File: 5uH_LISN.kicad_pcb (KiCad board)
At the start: 2 copper layers, 112.4 x 60.5 mm, 78 parts, among them J1 Conn_Coaxial, J2 Conn_Coaxial, J3 BANANA_CONN, J4 BANANA_CONN, J5 BANANA_CONN, J6 BANANA_CONN, J7 BANANA_CONN, J8 BANANA_CONN

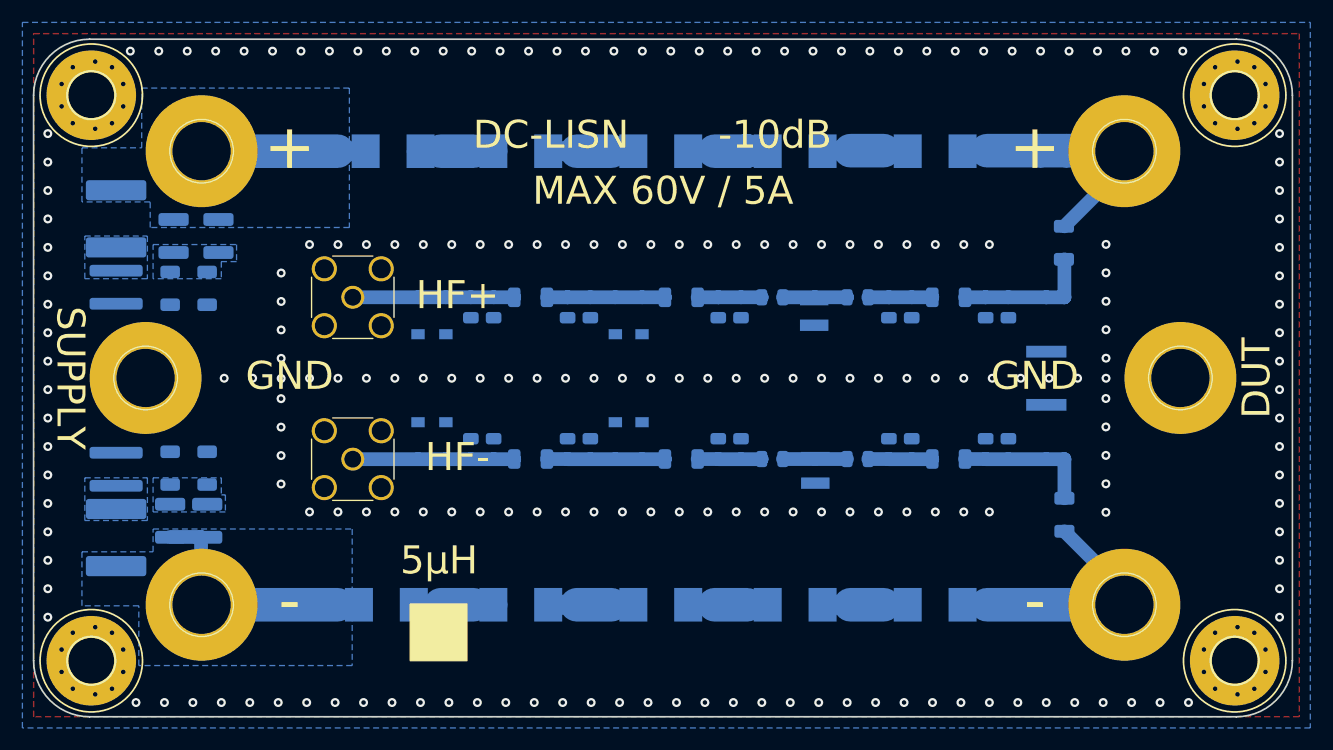
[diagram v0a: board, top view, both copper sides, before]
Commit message: LISN V1 R0 * Added simulation with LTSpice of the 10dB Attenuator / Transient Filter (with default 1N4148 and BAV99) * Replaced some 1N4148W by BAV99 from Nexperia (to reach up to 400MHz flat 10dB Attenuator / Transient Filter) * Changed space to have 19.06mm between Supply / DUT "+" <=> "GND" <=> "-" => 4mm BANANA JACK for BNC adapter * Changed Keystone Electronics 575-4 which are too short for banana by Keystone Electronics 575-8
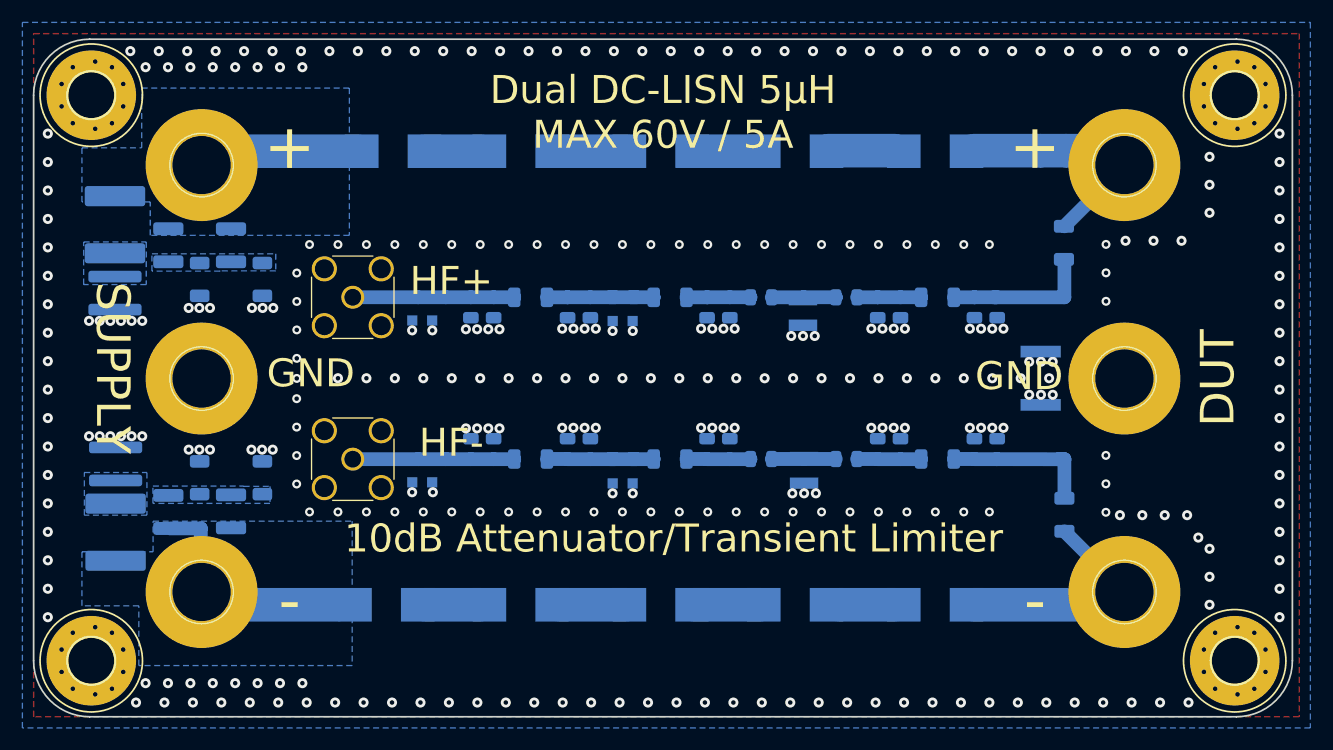
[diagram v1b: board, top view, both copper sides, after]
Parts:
- removed D5, D6, D7, D8: 1N4148W, Diode_SMD:D_SOD-123
- D1, D2, D3, D4: value 1N4148W -> SOT23-DIODEDUAL; footprint Diode_SMD:D_SOD-123 -> 5uH_LISN:SOT23-DIODEDUAL
- J1, J2: value Conn_Coaxial -> Conn_SMA
- moved D2 21.7 mm to (152.7, 104.1), turned to 0 degrees
- moved D4 16.0 mm to (152.7, 118.6), turned to 0 degrees
- moved D3 14.0 mm to (134.8, 118.5), turned to 0 degrees
- moved R14 5.01 mm to (120.5, 119.1)
- moved J4 5.00 mm to (115.1, 110.3)
- moved J6 5.00 mm to (197.5, 110.3)
- moved R9 5.00 mm to (120.5, 101.4)
- moved R31 3.03 mm to (184.1, 103.9)
- moved R10 2.77 mm to (114.9, 119.1)
- moved R13 2.75 mm to (114.9, 101.4)
- moved C8 2.29 mm to (117.7, 122.1)
- moved C5 1.39 mm to (117.7, 98.4)
- moved J3 1.24 mm to (115.1, 91.2)
- moved J7 1.24 mm to (197.5, 91.2)
- moved J5 1.14 mm to (115.1, 129.3)
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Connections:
- D1 pad 1: Net-(D1-Pad1) -> GND
- D2 pad 1: Net-(D2-Pad1) -> GND
- D3 pad 2: Net-(D1-Pad1) -> GND
- D4 pad 2: Net-(D2-Pad1) -> GND
- J1 pad 1: Net-(D1-Pad1) -> Net-(D1-Pad3)
- J2 pad 1: Net-(D2-Pad1) -> Net-(D3-Pad3)
- R1 pad 2: Net-(D1-Pad1) -> Net-(D1-Pad3)
- R11 pad 2: Net-(D5-Pad1) -> Net-(D2-Pad3)
- R12 pad 2: Net-(D6-Pad1) -> Net-(D4-Pad3)
- R15 pad 2: Net-(D5-Pad1) -> Net-(D2-Pad3)
- R16 pad 2: Net-(D6-Pad1) -> Net-(D4-Pad3)
- R17 pad 1: Net-(D5-Pad1) -> Net-(D2-Pad3)
- R18 pad 1: Net-(D6-Pad1) -> Net-(D4-Pad3)
- R2 pad 2: Net-(D2-Pad1) -> Net-(D3-Pad3)
- R5 pad 2: Net-(D1-Pad1) -> Net-(D1-Pad3)
- R6 pad 2: Net-(D2-Pad1) -> Net-(D3-Pad3)
- R7 pad 1: Net-(D1-Pad1) -> Net-(D1-Pad3)
- R7 pad 2: Net-(D5-Pad1) -> Net-(D2-Pad3)
- R8 pad 1: Net-(D2-Pad1) -> Net-(D3-Pad3)
- R8 pad 2: Net-(D6-Pad1) -> Net-(D4-Pad3)
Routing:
- net Net-(D3-Pad3): track 0.00 -> 14.4 mm
- net Net-(D2-Pad1): track 14.4 -> 0.00 mm
- net Net-(D1-Pad3): track 0.00 -> 14.4 mm
- net Net-(D1-Pad1): track 14.4 -> 0.00 mm
- net Net-(D6-Pad1): track 10.5 -> 0.00 mm
- net Net-(D4-Pad3): track 0.00 -> 10.5 mm
- net Net-(D5-Pad1): track 10.5 -> 0.00 mm
- net Net-(D2-Pad3): track 0.00 -> 10.5 mm
- net Net-(L7-Pad2): track 7.24 -> 5.00 mm
- net Net-(L1-Pad2): track 7.24 -> 5.00 mm
- net Net-(L10-Pad2): track 7.30 -> 9.30 mm
- net Net-(C15-Pad1): track 24.1 -> 22.4 mm
- net Net-(C16-Pad2): track 12.4 -> 13.8 mm
- net Net-(L8-Pad2): track 7.41 -> 6.00 mm
- net Net-(L2-Pad2): track 7.41 -> 6.00 mm
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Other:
- board text added: "10dB Attenuator/Transient Limiter"
- board text added: "Dual DC-LISN 5µH"
- board text added: "V1 R0 05Dec2021"
- board text removed: "-10dB"
- board text removed: "5µH"
- board text removed: "DC-LISN"

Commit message: Fixed issue https://github.com/bvernoux/EMC_5uH_LISN/issues/4 Remove bottom layer soldermask on PCB edge for proper grounding to case
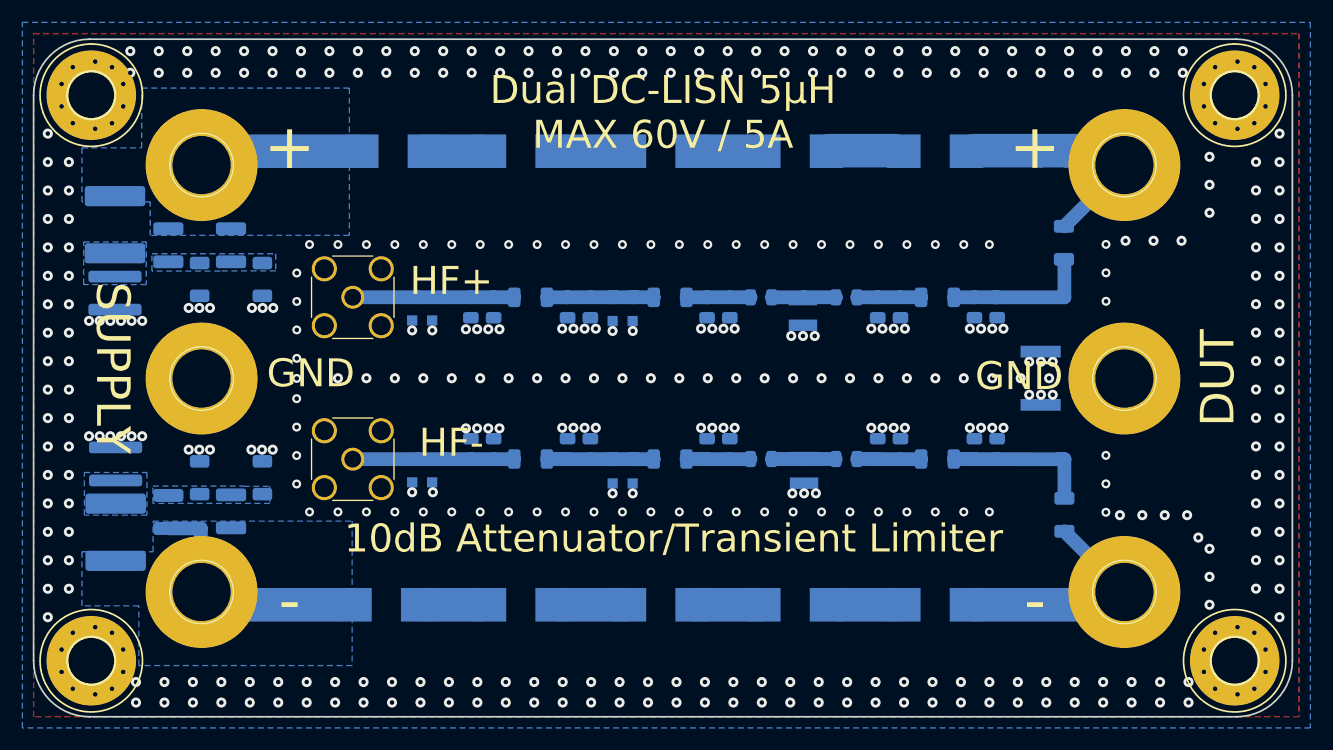
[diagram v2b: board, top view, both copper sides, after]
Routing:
- net GND: vias 357 -> 449
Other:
- board text added: "V1 R0 12Dec2021"
- board text removed: "V1 R0 05Dec2021"
